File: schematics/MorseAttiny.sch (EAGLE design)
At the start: 12 parts, among them Q1 500mA/300V

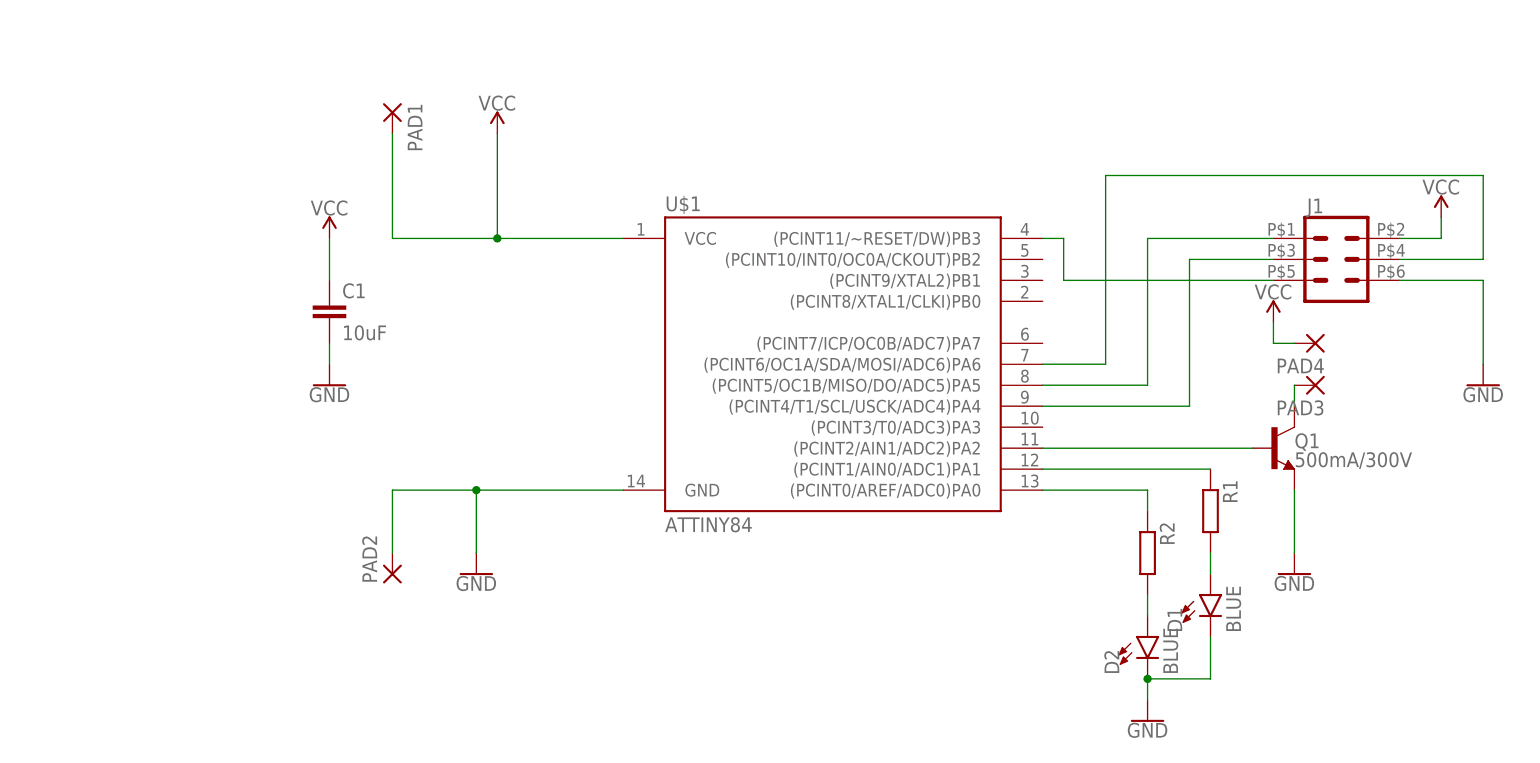
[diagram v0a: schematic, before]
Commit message: Major changes in Illustrator design and first silkscreen experiments
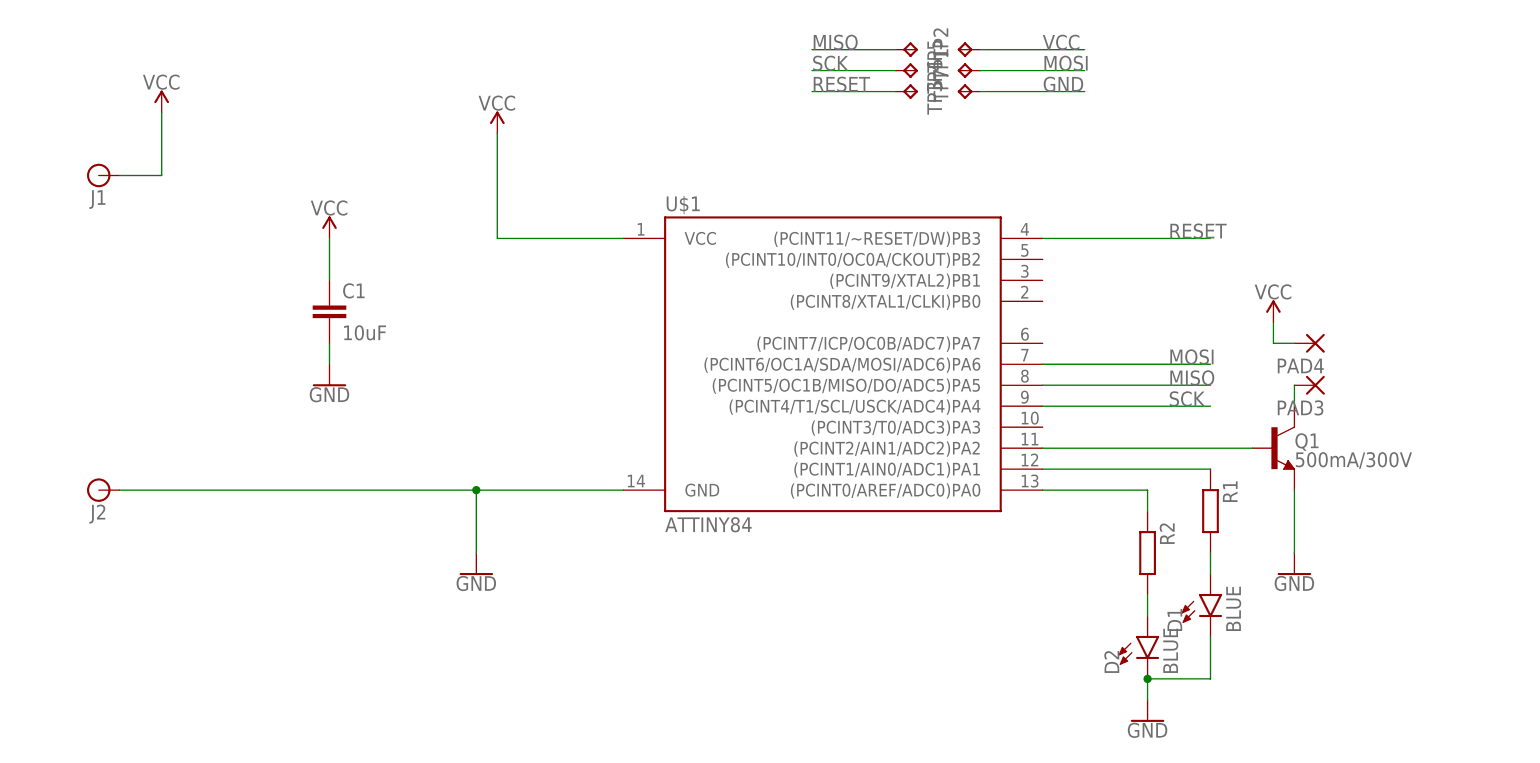
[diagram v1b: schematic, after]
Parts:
- removed PAD1, PAD2: (no value), wirepad:2,54/1,0
- added J2: (no value), SparkFun-Connectors:BANANA_CONN
- added TP1, TP2, TP3, TP4, TP5, TP7: TPTP18R, testpad:TPTP18R
- J1: device SparkFun-Connectors:CONN_03X2POGO_PINS -> SparkFun-Connectors:BANANA_CONN
- R1, R2: device rcl:R-EU_M1206 -> rcl:R-EU_M0805
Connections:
- net GND: now also J2.1, TP7.TP; no longer J1.6, PAD2.P
- net MISO: now also TP5.TP; no longer J1.1
- net MOSI: now also TP1.TP; no longer J1.4
- net RESET: now also TP3.TP; no longer J1.5
- net SCK: now also TP4.TP; no longer J1.3
- net VCC: now also J1.1, TP2.TP; no longer J1.2, PAD1.P

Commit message: changed pads to polygon areas, added eagle up renderings, major re-design
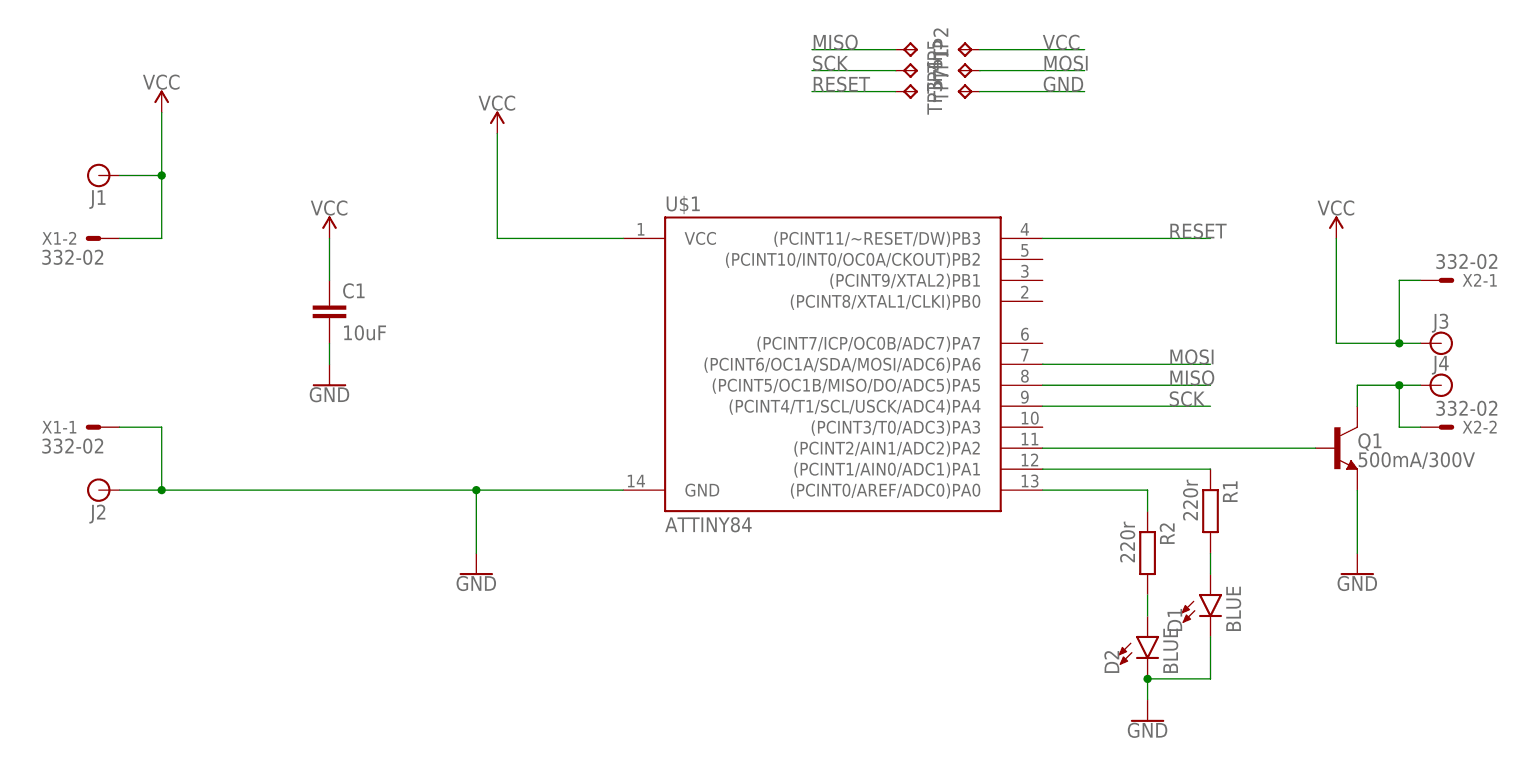
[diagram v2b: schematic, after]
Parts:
- removed PAD3, PAD4: (no value), wirepad:2,54/1,0
- added J3, J4: (no value), SparkFun-Connectors:BANANA_CONN
- added X1, X2: 332-02, con-garry:332-02
- R1, R2: value (none) -> 220r
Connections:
- removed net N$7: PAD3.P, Q1.C
- new net SPK: J4.1, Q1.C, X2-2.S
- net GND: now also X1-1.S
- net VCC: now also J3.1, X1-2.S, X2-1.S; no longer PAD4.P
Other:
- moved on the sheet: Q1
